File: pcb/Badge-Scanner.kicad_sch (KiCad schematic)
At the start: 26 parts, among them J2 Serial, J3 NFC-Module, J4 I2C, M1 Fan, Q3 AO3400A, U1 Pico W, U2 DS3231MZ, U4 CJ431

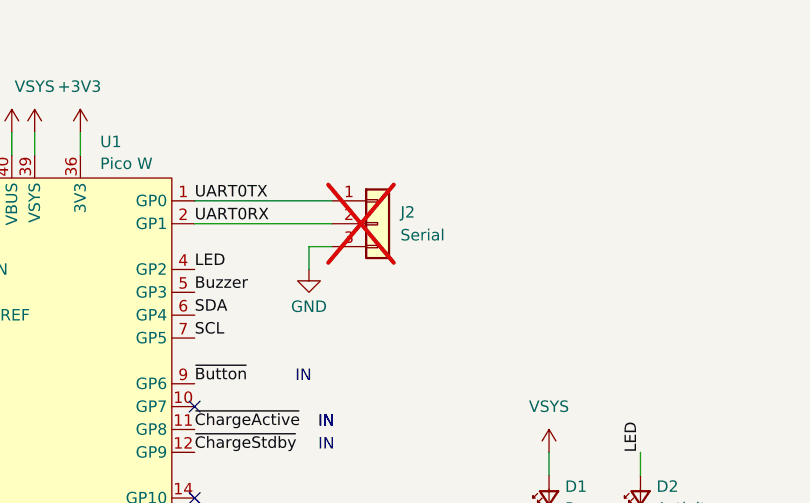
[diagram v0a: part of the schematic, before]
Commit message: fix: turn around UART connector
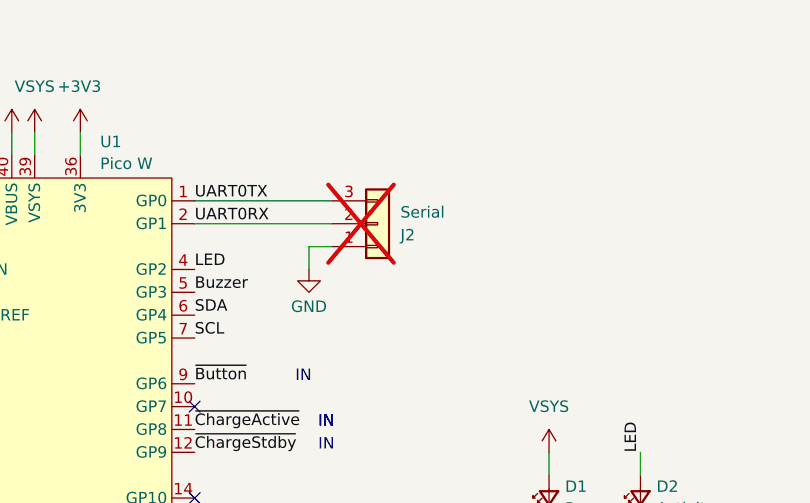
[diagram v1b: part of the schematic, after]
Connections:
- net GND: now also J2.1 (Pin_1); no longer J2.3 (Pin_3)
- net UART0TX: now also J2.3 (Pin_3); no longer J2.1 (Pin_1)
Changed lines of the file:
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@@
 		(lib_id "Connector_Generic:Conn_01x03")
 		(at 111.76 40.64 0)
+		(mirror x)
 		(unit 1)
 		(exclude_from_sim no)
@@
 		(on_board yes)
 		(dnp yes)
-		(fields_autoplaced yes)
 		(property "Reference" "J2"
-			(at 114.3 39.3699 0)
+			(at 114.3 41.9101 0)
 			(effects
 				(font
@@
 		)
 		(property "Value" "Serial"
-			(at 114.3 41.9099 0)
+			(at 114.3 39.3701 0)
 			(effects
 				(font

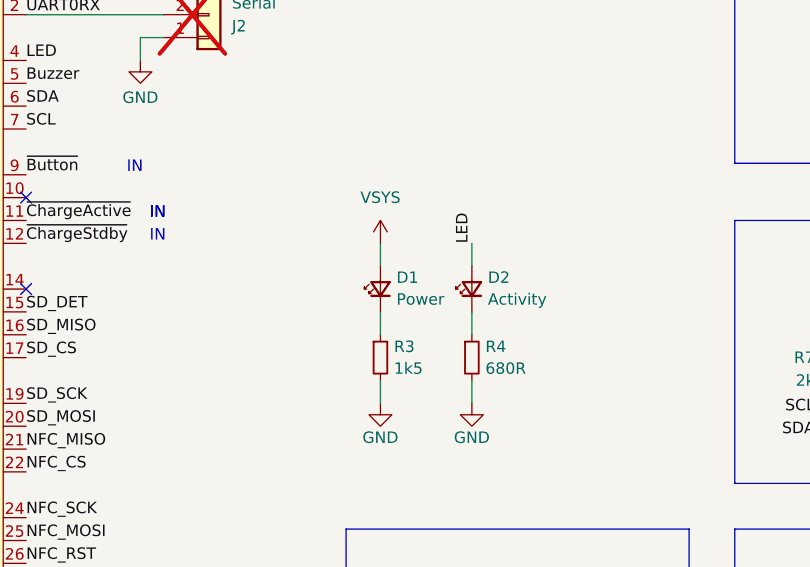
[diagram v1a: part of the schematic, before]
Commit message: fix: move power LED to 3.3V rail
VSYS is too unstable since its voltage changes a lot between usb and battery powered mode
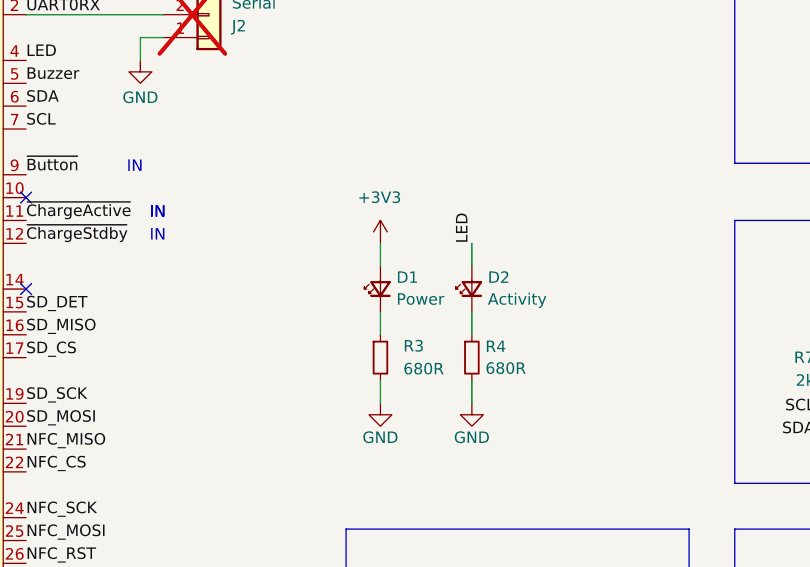
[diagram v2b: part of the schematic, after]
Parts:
- R3: value 1k5 -> 680R; LCSC C25867 -> C25130
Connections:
- net +3V3: now also D1.2 (A)
- net VSYS: no longer D1.2 (A)
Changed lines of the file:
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@@
-	)
-	(symbol
-		(lib_id "Badge-Scanner:VSYS")
-		(at 130.81 66.04 0)
-		(unit 1)
-		(exclude_from_sim no)
-		(in_bom no)
-		(on_board no)
-		(dnp no)
-		(fields_autoplaced yes)
-		(property "Reference" "#PWR07"
-			(at 130.81 66.04 0)
-			(effects
-				(font
-					(size 1.27 1.27)
-				)
-				(hide yes)
-			)
-		)
-		(property "Value" "VSYS"
-			(at 130.81 60.96 0)
-			(effects
-				(font
-					(size 1.27 1.27)
-				)
-			)
-		)
-		(property "Footprint" ""
-			(at 130.81 66.04 0)
-			(effects
-				(font
-					(size 1.27 1.27)
-				)
-				(hide yes)
-			)
-		)
-		(property "Datasheet" ""
-			(at 130.81 66.04 0)
-			(effects
-				(font
-					(size 1.27 1.27)
-				)
-				(hide yes)
-			)
-		)
-		(property "Description" ""
-			(at 130.81 66.04 0)
-			(effects
-				(font
-					(size 1.27 1.27)
-				)
-				(hide yes)
-			)
-		)
-		(pin ""
-		)
-		(instances
-			(project ""
-				(path "/e99cd76d-c117-4654-ad48-596a9e3de149"
-					(reference "#PWR07")
-					(unit 1)
-				)
-			)
-		)
 	)
 	(symbol
@@
 	(symbol
 		(lib_id "power:+3V3")
+		(at 130.81 66.04 0)
+		(unit 1)
+		(exclude_from_sim no)
+		(in_bom yes)
+		(on_board yes)
+		(dnp no)
+		(property "Reference" "#PWR07"
+			(at 130.81 69.85 0)
+			(effects
+				(font
+					(size 1.27 1.27)
+				)
+				(hide yes)
+			)
+		)
+		(property "Value" "+3V3"
+			(at 128.27 60.96 0)
+			(effects
+				(font
+					(size 1.27 1.27)
+				)
+				(justify left)
+			)
+		)
+		(property "Footprint" ""
+			(at 130.81 66.04 0)
+			(effects
+				(font
+					(size 1.27 1.27)
+				)
+				(hide yes)
+			)
+		)
+		(property "Datasheet" ""
+			(at 130.81 66.04 0)
+			(effects
+				(font
+					(size 1.27 1.27)
+				)
+				(hide yes)
+			)
+		)
+		(property "Description" "Power symbol creates a global label with name \"+3V3\""
+			(at 130.81 66.04 0)
+			(effects
+				(font
+					(size 1.27 1.27)
+				)
+				(hide yes)
+			)
+		)
+		(pin "1"
+		)
+		(instances
+			(project "Badge-Scanner"
+				(path "/e99cd76d-c117-4654-ad48-596a9e3de149"
+					(reference "#PWR07")
+					(unit 1)
+				)
+			)
+		)
+	)
+	(symbol
+		(lib_id "power:+3V3")
 		(at 144.78 109.22 0)
 		(unit 1)
@@
 		(fields_autoplaced yes)
 		(property "Reference" "R3"
-			(at 132.3086 77.5279 0)
+			(at 133.35 77.4699 0)
 			(effects
 				(font
@@
 			)
 		)
-		(property "Value" "1k5"
-			(at 132.3086 79.9521 0)
+		(property "Value" "680R"
+			(at 133.35 80.0099 0)
 			(effects
 				(font
@@
 			)
 		)
-		(property "LCSC" "C25867"
+		(property "LCSC" "C25130"
 			(at 130.81 78.74 0)
 			(effects

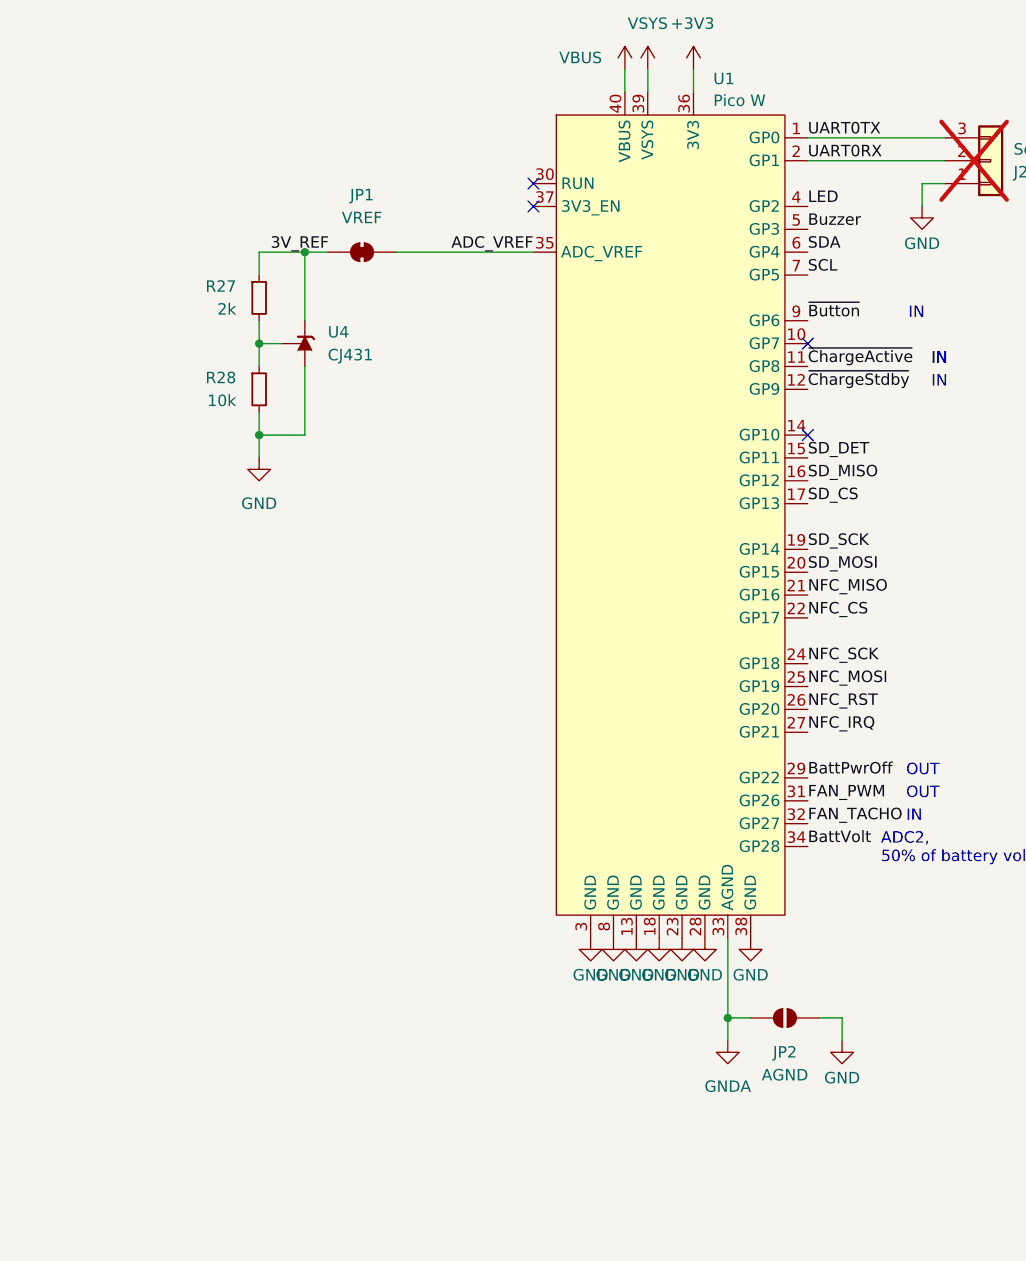
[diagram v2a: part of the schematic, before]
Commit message: fix: add caps to delay startup of mcu
Sometimes the mcu does not boot correctly when usb gets connected while the system is off - most likely because the flash does not get enough power quick enough. Adding a startup delay for the 3V3 regulator and the mcu itself helps in my tests. This delays the boot by about half a second.
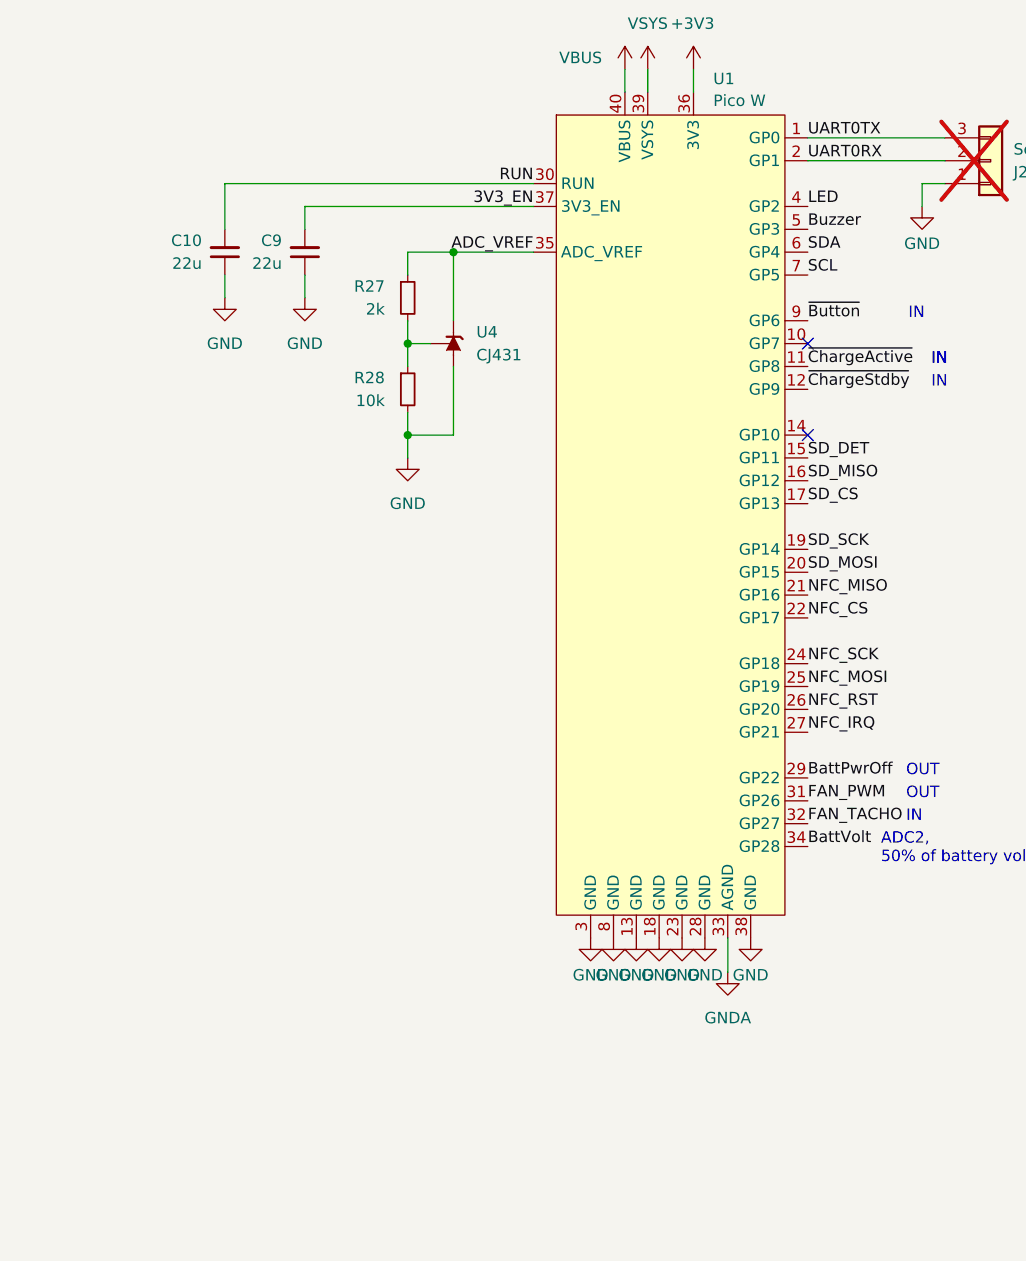
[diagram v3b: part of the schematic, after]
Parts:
- removed JP1: VREF, Jumper:SolderJumper-2_P1.3mm_Bridged_RoundedPad1.0x1.5mm, symbol Jumper:SolderJumper_2_Bridged
- removed JP2: AGND, Jumper:SolderJumper-2_P1.3mm_Open_RoundedPad1.0x1.5mm, symbol Jumper:SolderJumper_2_Open
- added C10, C9: 22u, Capacitor_SMD:C_0603_1608Metric, symbol Device:C_Small
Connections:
- net 3V_REF is gone; now on net ADC_VREF: R27.1, U4.2 (K)
- net GND: now also C10.1, C9.1
- net RUN: now reaches U1.30 (RUN)
- net RUN: now also C10.2
- net 3V3_EN: now reaches U1.37 (3V3_EN)
- net 3V3_EN: now also C9.2
- no-connect marks 7 -> 5
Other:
- moved on the sheet: R27, R28, U4
